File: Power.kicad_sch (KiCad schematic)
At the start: 0 parts

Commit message: USB and PWR sch
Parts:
- added C2: 10u, symbol Device:C
- added C3, C5: 0.1u, symbol Device:C
- added C4: 33u, symbol Device:C
- added D5: PWR, symbol Device:LED
- added R3: TODO, symbol Device:R
- added U2: LM3940IMP-3.3/NOPB, MP04A, symbol LM3940IMP:LM3940IMP-3.3_NOPB
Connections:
- new net: D5.2 (A), R3.2
- new net +3.3v: C4.1, C5.1, R3.1, U2.3 (OUT)
- new net +5V: C2.1, C3.1, U2.1 (IN)
- new net GND: C2.2, C3.2, C4.2, C5.2, D5.1 (K), U2.2 (GND), U2.4 (GND)
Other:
- title: (none) -> Power

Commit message: finished sch? (need P/Ns)
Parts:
- added D6: PWR, symbol Device:LED
- added R7: TODO, symbol Device:R
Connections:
- net +3.3v: now also R7.1
- net GND: now also D6.1 (K)
- new net: D6.2 (A), R7.2
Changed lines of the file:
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@@
+	(wire
+		(pts
+			(xy 153.67 29.21) (xy 153.67 31.75)
+		)
+		(stroke
+			(width 0)
+			(type default)
+		)
+	)
 	(wire
 		(pts
@@
 	(wire
 		(pts
+			(xy 153.67 39.37) (xy 153.67 41.91)
+		)
+		(stroke
+			(width 0)
+			(type default)
+		)
+	)
+	(wire
+		(pts
 			(xy 101.6 43.18) (xy 101.6 45.72)
 		)
@@
 		(pts
 			(xy 113.03 43.18) (xy 113.03 45.72)
+		)
+		(stroke
+			(width 0)
+			(type default)
+		)
+	)
+	(wire
+		(pts
+			(xy 153.67 49.53) (xy 153.67 52.07)
 		)
 		(stroke
@@
 		(shape output)
 		(at 74.93 36.83 90)
+		(fields_autoplaced yes)
+		(effects
+			(font
+				(size 1.27 1.27)
+			)
+			(justify left)
+		)
+	)
+	(hierarchical_label "+3.3v"
+		(shape output)
+		(at 153.67 29.21 90)
 		(fields_autoplaced yes)
 		(effects
@@
 	)
 	(symbol
+		(lib_id "Device:R")
+		(at 153.67 35.56 0)
+		(unit 1)
+		(exclude_from_sim no)
+		(in_bom yes)
+		(on_board yes)
+		(dnp no)
+		(fields_autoplaced yes)
+		(property "Reference" "R7"
+			(at 156.21 34.2899 0)
+			(effects
+				(font
+					(size 1.27 1.27)
+				)
+				(justify left)
+			)
+		)
+		(property "Value" "TODO"
+			(at 156.21 36.8299 0)
+			(effects
+				(font
+					(size 1.27 1.27)
+				)
+				(justify left)
+			)
+		)
+		(property "Footprint" ""
+			(at 151.892 35.56 90)
+			(effects
+				(font
+					(size 1.27 1.27)
+				)
+				(hide yes)
+			)
+		)
+		(property "Datasheet" "~"
+			(at 153.67 35.56 0)
+			(effects
+				(font
+					(size 1.27 1.27)
+				)
+				(hide yes)
+			)
+		)
+		(property "Description" "Resistor"
+			(at 153.67 35.56 0)
+			(effects
+				(font
+					(size 1.27 1.27)
+				)
+				(hide yes)
+			)
+		)
+		(pin "1"
+		)
+		(pin "2"
+		)
+		(instances
+			(project "esp32-devboard"
+				(path "/0204cec0-d71e-48a7-8736-ccb0d3e9b02c/bacb3f46-de5d-435f-80be-a3240178eb39"
+					(reference "R7")
+					(unit 1)
+				)
+			)
+		)
+	)
+	(symbol
 		(lib_id "power:GND")
 		(at 140.97 52.07 0)
@@
 	)
 	(symbol
+		(lib_id "Device:LED")
+		(at 153.67 45.72 90)
+		(unit 1)
+		(exclude_from_sim no)
+		(in_bom yes)
+		(on_board yes)
+		(dnp no)
+		(fields_autoplaced yes)
+		(property "Reference" "D6"
+			(at 157.48 46.0374 90)
+			(effects
+				(font
+					(size 1.27 1.27)
+				)
+				(justify right)
+			)
+		)
+		(property "Value" "PWR"
+			(at 157.48 48.5774 90)
+			(effects
+				(font
+					(size 1.27 1.27)
+				)
+				(justify right)
+			)
+		)
+		(property "Footprint" ""
+			(at 153.67 45.72 0)
+			(effects
+				(font
+					(size 1.27 1.27)
+				)
+				(hide yes)
+			)
+		)
+		(property "Datasheet" "~"
+			(at 153.67 45.72 0)
+			(effects
+				(font
+					(size 1.27 1.27)
+				)
+				(hide yes)
+			)
+		)
+		(property "Description" "Light emitting diode"
+			(at 153.67 45.72 0)
+			(effects
+				(font
+					(size 1.27 1.27)
+				)
+				(hide yes)
+			)
+		)
+		(pin "2"
+		)
+		(pin "1"
+		)
+		(instances
+			(project "esp32-devboard"
+				(path "/0204cec0-d71e-48a7-8736-ccb0d3e9b02c/bacb3f46-de5d-435f-80be-a3240178eb39"
+					(reference "D6")
+					(unit 1)
+				)
+			)
+		)
+	)
+	(symbol
 		(lib_id "power:GND")
 		(at 74.93 44.45 0)
@@
 					(unit 1)
 				)
+			)
+		)
+	)
+	(symbol
+		(lib_id "power:GND")
+		(at 153.67 52.07 0)
+		(unit 1)
+		(exclude_from_sim no)
+		(in_bom yes)
+		(on_board yes)
+		(dnp no)
+		(fields_autoplaced yes)
+		(property "Reference" "#PWR029"
+			(at 153.67 58.42 0)
+			(effects
+				(font
+					(size 1.27 1.27)
+				)
+				(hide yes)
+			)
+		)
+		(property "Value" "GND"
+			(at 153.67 57.15 0)
+			(effects
+				(font
+					(size 1.27 1.27)
+				)
+			)
+		)
+		(property "Footprint" ""
+			(at 153.67 52.07 0)
+			(effects
+				(font
+					(size 1.27 1.27)
+				)
+				(hide yes)
+			)
+		)
+		(property "Datasheet" ""
+			(at 153.67 52.07 0)
+			(effects
+				(font
+					(size 1.27 1.27)
+				)
+				(hide yes)
+			)
+		)
+		(property "Description" "Power symbol creates a global label with name \"GND\" , ground"
+			(at 153.67 52.07 0)
+			(effects
+				(font
+					(size 1.27 1.27)
+				)
+				(hide yes)
+			)
+		)
+		(pin "1"
+		)
+		(instances
+			(project "esp32-devboard"
+				(path "/0204cec0-d71e-48a7-8736-ccb0d3e9b02c/bacb3f46-de5d-435f-80be-a3240178eb39"
+					(reference "#PWR029")
+					(unit 1)
+				)

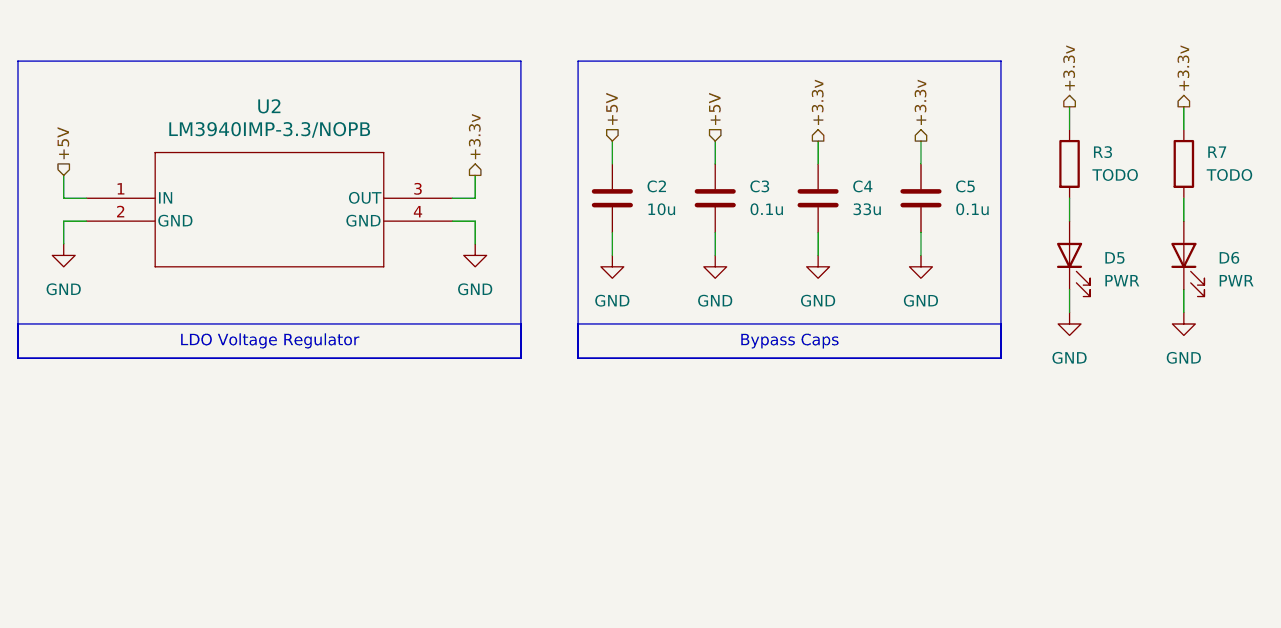
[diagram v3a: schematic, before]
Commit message: add P/N
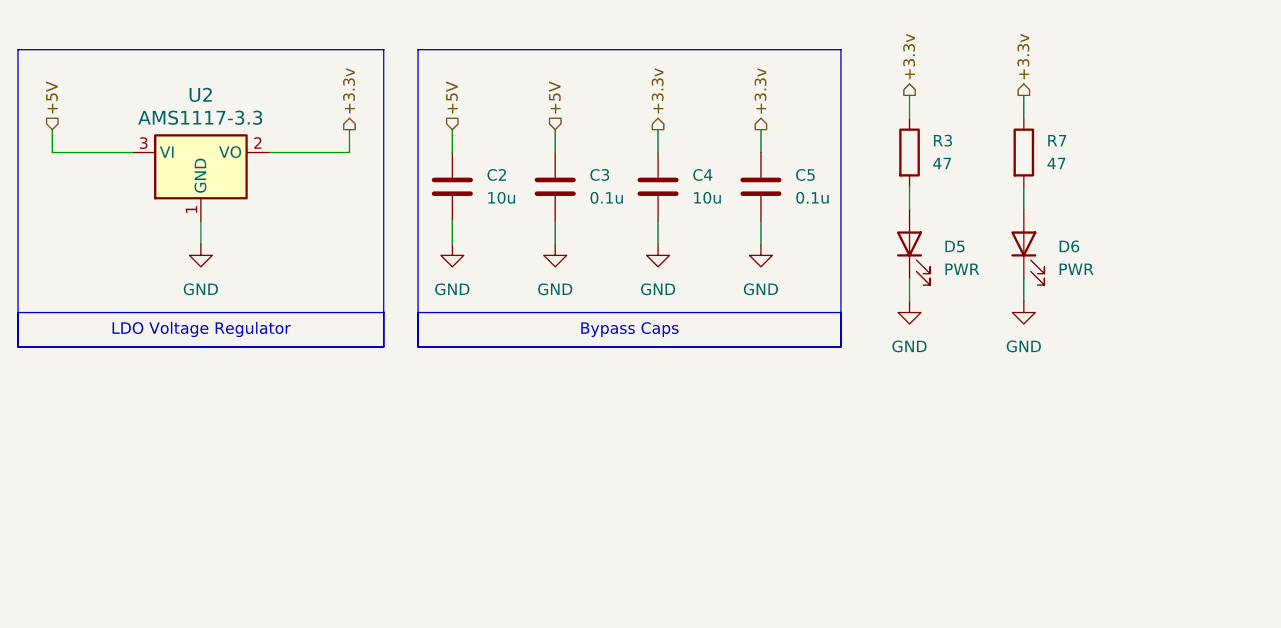
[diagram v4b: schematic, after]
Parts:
- C2: P/N (none) -> MLAST168BB5106MTNA01
- C3, C5: P/N (none) -> C0603G104K5RACT250
- C4: value 33u -> 10u; P/N (none) -> MLAST168BB5106MTNA01
- D5, D6: P/N (none) -> HSML-C191
- R3, R7: value TODO -> 47; P/N (none) -> MCT06030C4709FP500
- U2: value LM3940IMP-3.3/NOPB -> AMS1117-3.3; footprint MP04A -> Package_TO_SOT_SMD:SOT-223-3_TabPin2; symbol LM3940IMP:LM3940IMP-3.3_NOPB -> Regulator_Linear:AMS1117-3.3; P/N (none) -> AMS1117-3.3
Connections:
- net +3.3v: now also U2.2 (VO); no longer U2.3 (OUT)
- net +5V: now also U2.3 (VI); no longer U2.1 (IN)
- net GND: now also U2.1 (GND); no longer U2.2 (GND), U2.4 (GND)
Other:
- moved on the sheet: C2, C3, C5, D5, D6, R3, R7

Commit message: assign footprints
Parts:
- C2, C3, C4, C5: footprint (none) -> Capacitor_SMD:C_0603_1608Metric
- D5, D6: footprint (none) -> LED_SMD:LED_0603_1608Metric
- R3, R7: footprint (none) -> Resistor_SMD:R_0603_1608Metric
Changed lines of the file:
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@@
 			)
 		)
-		(property "Footprint" ""
+		(property "Footprint" "Capacitor_SMD:C_0603_1608Metric"
 			(at 96.2152 41.91 0)
 			(effects
@@
 			)
 		)
-		(property "Footprint" ""
+		(property "Footprint" "Capacitor_SMD:C_0603_1608Metric"
 			(at 107.6452 41.91 0)
 			(effects
@@
 			)
 		)
-		(property "Footprint" ""
+		(property "Footprint" "Capacitor_SMD:C_0603_1608Metric"
 			(at 84.7852 41.91 0)
 			(effects
@@
 			)
 		)
-		(property "Footprint" ""
+		(property "Footprint" "Resistor_SMD:R_0603_1608Metric"
 			(at 134.112 34.29 90)
 			(effects
@@
 			)
 		)
-		(property "Footprint" ""
+		(property "Footprint" "LED_SMD:LED_0603_1608Metric"
 			(at 135.89 44.45 0)
 			(effects
@@
 			)
 		)
-		(property "Footprint" ""
+		(property "Footprint" "Capacitor_SMD:C_0603_1608Metric"
 			(at 73.3552 41.91 0)
 			(effects
@@
 			)
 		)
-		(property "Footprint" ""
+		(property "Footprint" "LED_SMD:LED_0603_1608Metric"
 			(at 123.19 44.45 0)
 			(effects
@@
 			)
 		)
-		(property "Footprint" ""
+		(property "Footprint" "Resistor_SMD:R_0603_1608Metric"
 			(at 121.412 34.29 90)
 			(effects

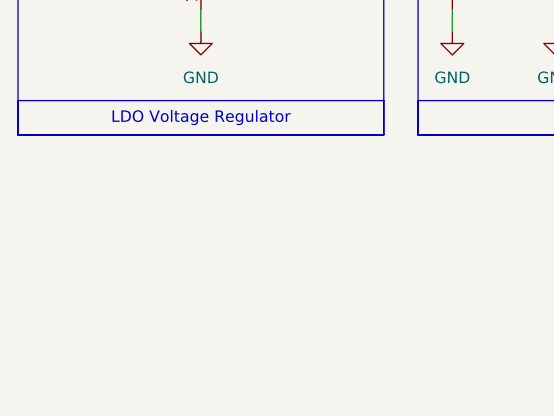
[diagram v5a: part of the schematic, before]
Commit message: add testpoints
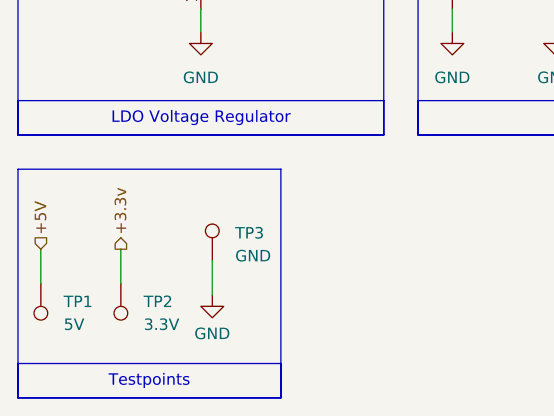
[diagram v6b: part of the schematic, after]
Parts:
- added TP1: 5V, symbol Connector:TestPoint
- added TP2: 3.3V, symbol Connector:TestPoint
- added TP3: GND, symbol Connector:TestPoint
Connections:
- net +3.3v: now also TP2.1
- net +5V: now also TP1.1
- net GND: now also TP3.1

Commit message: LDO layout>
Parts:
- TP1, TP2, TP3: footprint (none) -> TestPoint:TestPoint_Pad_D1.0mm
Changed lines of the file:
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@@
 			)
 		)
-		(property "Footprint" ""
+		(property "Footprint" "TestPoint:TestPoint_Pad_D1.0mm"
 			(at 50.8 69.85 0)
 			(effects
@@
 			)
 		)
-		(property "Footprint" ""
+		(property "Footprint" "TestPoint:TestPoint_Pad_D1.0mm"
 			(at 21.59 72.39 0)
 			(effects
@@
 			)
 		)
-		(property "Footprint" ""
+		(property "Footprint" "TestPoint:TestPoint_Pad_D1.0mm"
 			(at 30.48 72.39 0)
 			(effects

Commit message: layout kinda done
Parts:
- removed TP1: 5V, TestPoint:TestPoint_Pad_D1.0mm, symbol Connector:TestPoint
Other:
- moved on the sheet: TP2, TP3
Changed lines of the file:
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@@
 	(wire
 		(pts
-			(xy 35.56 68.58) (xy 35.56 72.39)
+			(xy 31.75 68.58) (xy 31.75 72.39)
 		)
 		(stroke
@@
 	(wire
 		(pts
-			(xy 26.67 68.58) (xy 26.67 72.39)
-		)
-		(stroke
-			(width 0)
-			(type default)
-		)
-	)
-	(wire
-		(pts
 			(xy 27.94 34.29) (xy 36.83 34.29)
 		)
@@
 	(wire
 		(pts
-			(xy 45.72 69.85) (xy 45.72 73.66)
+			(xy 41.91 69.85) (xy 41.91 73.66)
 		)
 		(stroke
@@
 	(hierarchical_label "+3.3v"
 		(shape output)
-		(at 35.56 68.58 90)
+		(at 31.75 68.58 90)
 		(fields_autoplaced yes)
 		(effects
@@
 		(shape input)
 		(at 27.94 31.75 90)
-		(fields_autoplaced yes)
-		(effects
-			(font
-				(size 1.27 1.27)
-			)
-			(justify left)
-		)
-	)
-	(hierarchical_label "+5V"
-		(shape input)
-		(at 26.67 68.58 90)
 		(fields_autoplaced yes)
 		(effects
@@
 	(symbol
 		(lib_id "Connector:TestPoint")
-		(at 45.72 69.85 0)
+		(at 41.91 69.85 0)
 		(unit 1)
 		(exclude_from_sim no)
@@
 		(dnp no)
 		(property "Reference" "TP3"
-			(at 48.26 66.802 0)
+			(at 44.45 66.802 0)
 			(effects
 				(font
@@
 		)
 		(property "Value" "GND"
-			(at 48.26 69.342 0)
+			(at 44.45 69.342 0)
 			(effects
 				(font
@@
 		)
 		(property "Footprint" "TestPoint:TestPoint_Pad_D1.0mm"
-			(at 50.8 69.85 0)
+			(at 46.99 69.85 0)
 			(effects
 				(font
@@
 		)
 		(property "Datasheet" "~"
-			(at 50.8 69.85 0)
+			(at 46.99 69.85 0)
 			(effects
 				(font
@@
 		)
 		(property "Description" "test point"
-			(at 45.72 69.85 0)
+			(at 41.91 69.85 0)
 			(effects
 				(font
@@
 	)
 	(symbol
-		(lib_id "Connector:TestPoint")
-		(at 26.67 72.39 180)
-		(unit 1)
-		(exclude_from_sim no)
-		(in_bom yes)
-		(on_board yes)
-		(dnp no)
-		(fields_autoplaced yes)
-		(property "Reference" "TP1"
-			(at 29.21 74.4219 0)
-			(effects
-				(font
-					(size 1.27 1.27)
-				)
-				(justify right)
-			)
-		)
-		(property "Value" "5V"
-			(at 29.21 76.9619 0)
-			(effects
-				(font
-					(size 1.27 1.27)
-				)
-				(justify right)
-			)
-		)
-		(property "Footprint" "TestPoint:TestPoint_Pad_D1.0mm"
-			(at 21.59 72.39 0)
-			(effects
-				(font
-					(size 1.27 1.27)
-				)
-				(hide yes)
-			)
-		)
-		(property "Datasheet" "~"
-			(at 21.59 72.39 0)
-			(effects
-				(font
-					(size 1.27 1.27)
-				)
-				(hide yes)
-			)
-		)
-		(property "Description" "test point"
-			(at 26.67 72.39 0)
-			(effects
-				(font
-					(size 1.27 1.27)
-				)
-				(hide yes)
-			)
-		)
-		(pin "1"
-		)
-		(instances
-			(project ""
-				(path "/0204cec0-d71e-48a7-8736-ccb0d3e9b02c/bacb3f46-de5d-435f-80be-a3240178eb39"
-					(reference "TP1")
-					(unit 1)
-				)
-			)
-		)
-	)
-	(symbol
 		(lib_id "Device:R")
 		(at 135.89 34.29 0)
@@
 	(symbol
 		(lib_id "Connector:TestPoint")
-		(at 35.56 72.39 180)
+		(at 31.75 72.39 180)
 		(unit 1)
 		(exclude_from_sim no)
@@
 		(dnp no)
 		(property "Reference" "TP2"
-			(at 38.1 74.4219 0)
+			(at 34.29 74.4219 0)
 			(effects
 				(font
@@
 		)
 		(property "Value" "3.3V"
-			(at 38.1 76.9619 0)
+			(at 34.29 76.9619 0)
 			(effects
 				(font
@@
 		)
 		(property "Footprint" "TestPoint:TestPoint_Pad_D1.0mm"
-			(at 30.48 72.39 0)
+			(at 26.67 72.39 0)
 			(effects
 				(font
@@
 		)
 		(property "Datasheet" "~"
-			(at 30.48 72.39 0)
+			(at 26.67 72.39 0)
 			(effects
 				(font
@@
 		)
 		(property "Description" "test point"
-			(at 35.56 72.39 0)
+			(at 31.75 72.39 0)
 			(effects
 				(font
@@
 	(symbol
 		(lib_id "power:GND")
-		(at 45.72 73.66 0)
+		(at 41.91 73.66 0)
 		(unit 1)
 		(exclude_from_sim no)
@@
 		(dnp no)
 		(property "Reference" "#PWR011"
-			(at 45.72 80.01 0)
+			(at 41.91 80.01 0)
 			(effects
 				(font
@@
 		)
 		(property "Value" "GND"
-			(at 45.72 77.978 0)
+			(at 41.91 77.978 0)
 			(effects
 				(font
@@
 		)
 		(property "Footprint" ""
-			(at 45.72 73.66 0)
+			(at 41.91 73.66 0)
 			(effects
 				(font
@@
 		)
 		(property "Datasheet" ""
-			(at 45.72 73.66 0)
+			(at 41.91 73.66 0)
 			(effects
 				(font
@@
 		)
 		(property "Description" "Power symbol creates a global label with name \"GND\" , ground"
-			(at 45.72 73.66 0)
-			(effects
-				(font
+			(at 41.91 73.66 0)
+			(effects
+				(font
